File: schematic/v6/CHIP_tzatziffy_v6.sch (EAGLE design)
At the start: 51 parts, among them J1 2X20-CHIP0.8_DRILL, J3 S2B-PH-SM4-TB, Q1 NPN-DTC114YUA, Q2 PNP-DTA114YUA, U1 LMR62421, U3 DS2431P, X1 FH12-40S-0.5SH

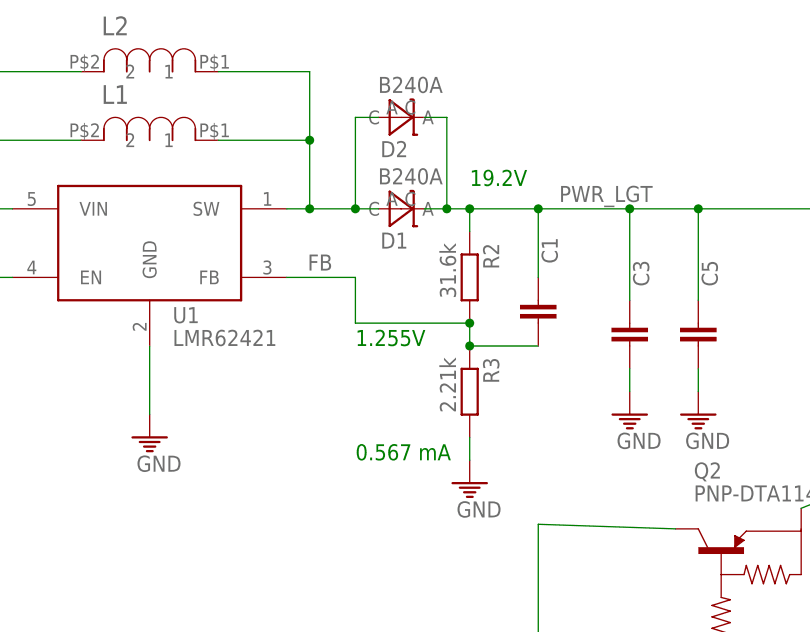
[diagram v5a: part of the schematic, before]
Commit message: added note for correct voltage divider
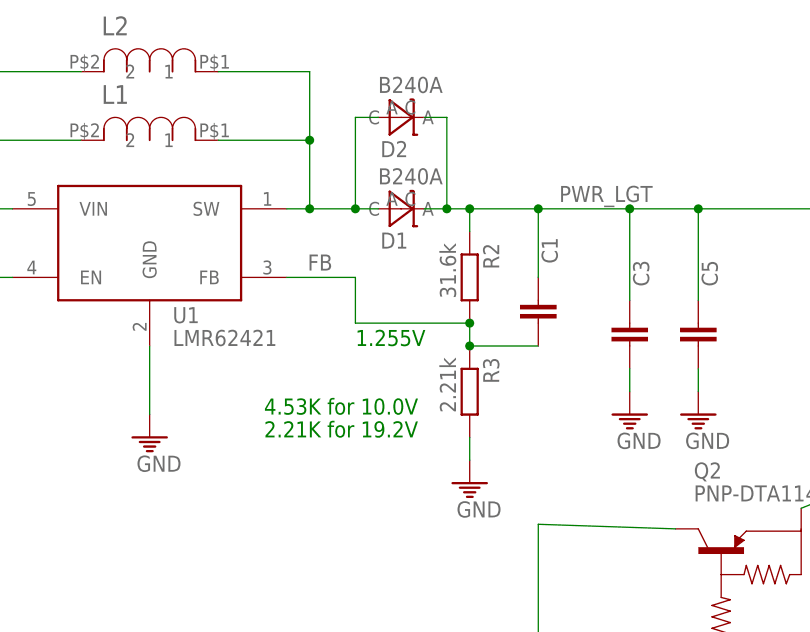
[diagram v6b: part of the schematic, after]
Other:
- note added: "2.21K for 19.2V"
- note added: "4.53K for 10.0V"
- note removed: "0.567 mA"
- note removed: "19.2V"
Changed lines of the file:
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@@
 <text x="236.22" y="81.28" size="1.778" layer="94" font="vector" ratio="12">1W EEPROM</text>
 <text x="530.86" y="246.38" size="1.778" layer="91">1.255V</text>
-<text x="543.56" y="264.16" size="1.778" layer="91">19.2V</text>
-<text x="530.86" y="233.68" size="1.778" layer="91">0.567 mA</text>
 <text x="363.22" y="246.38" size="1.778" layer="99">cut here</text>
 <text x="363.22" y="236.22" size="1.778" layer="99">cut here</text>
 <text x="449.58" y="243.84" size="1.778" layer="99" rot="R90">&lt;- cut here</text>
+<text x="520.7" y="238.76" size="1.778" layer="91">4.53K for 10.0V</text>
+<text x="520.7" y="236.22" size="1.778" layer="91">2.21K for 19.2V</text>
 </plain>
 <instances>

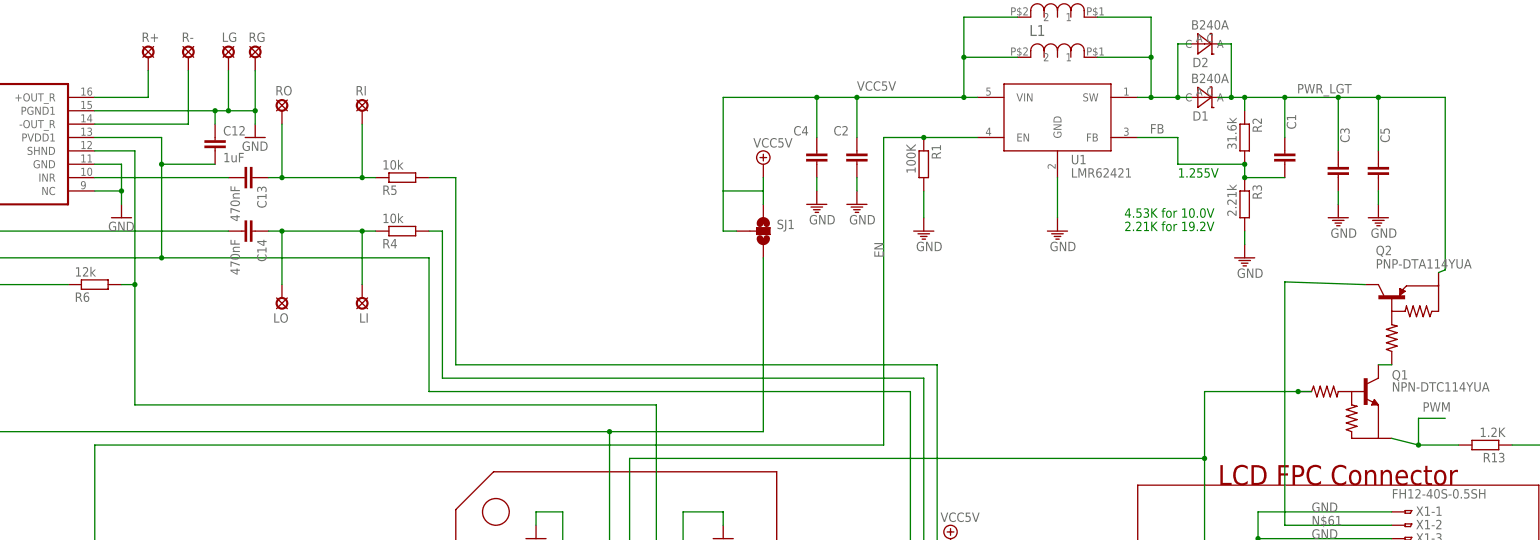
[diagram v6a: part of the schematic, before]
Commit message: changed 22uF Footprint to 1206
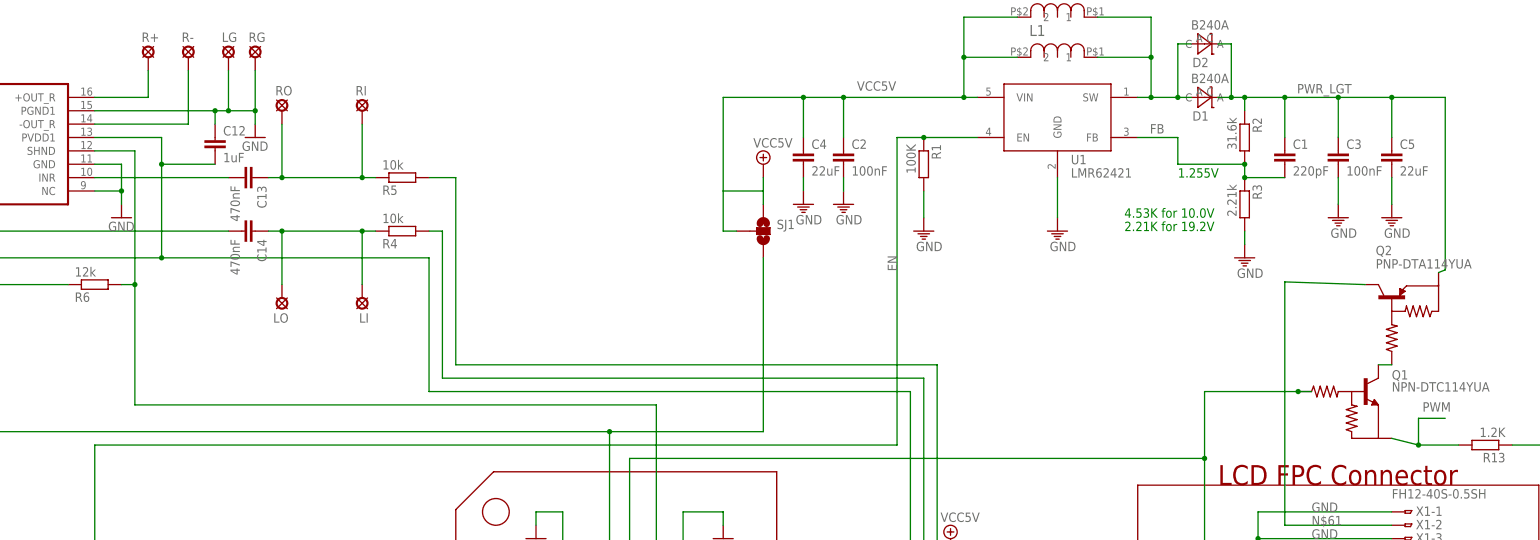
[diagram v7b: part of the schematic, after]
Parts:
- C4, C5: device rcl:C-EUC0805 -> rcl:C-EUC1206
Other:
- moved on the sheet: C2, C3, C4, C5
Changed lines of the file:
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@@
 <part name="U$13" library="Keyboard v0.2" deviceset="GND" device=""/>
 <part name="U$14" library="Keyboard v0.2" deviceset="GND" device=""/>
-<part name="C4" library="rcl" deviceset="C-EU" device="C0805" value="22uF"/>
-<part name="C5" library="rcl" deviceset="C-EU" device="C0805" value="22uF"/>
+<part name="C4" library="rcl" deviceset="C-EU" device="C1206" value="22uF"/>
+<part name="C5" library="rcl" deviceset="C-EU" device="C1206" value="22uF"/>
 <part name="U$15" library="Keyboard v0.2" deviceset="GND" device=""/>
 <part name="U$16" library="Keyboard v0.2" deviceset="GND" device=""/>
@@
 <instance part="U$8" gate="M" x="508" y="236.22"/>
 <instance part="U$12" gate="M" x="543.56" y="231.14"/>
-<instance part="C1" gate="G$1" x="551.18" y="251.46" smashed="yes">
-<attribute name="NAME" x="553.339" y="255.524" size="1.778" layer="95" rot="R90"/>
-</instance>
-<instance part="C2" gate="G$1" x="469.9" y="251.46" smashed="yes">
-<attribute name="NAME" x="468.376" y="256.159" size="1.778" layer="95" rot="R180"/>
-</instance>
-<instance part="C3" gate="G$1" x="561.34" y="248.92" smashed="yes">
-<attribute name="NAME" x="563.499" y="252.984" size="1.778" layer="95" rot="R90"/>
-</instance>
+<instance part="C1" gate="G$1" x="551.18" y="251.46"/>
+<instance part="C2" gate="G$1" x="467.36" y="251.46"/>
+<instance part="C3" gate="G$1" x="561.34" y="251.46"/>
 <instance part="U$13" gate="M" x="561.34" y="238.76"/>
-<instance part="U$14" gate="M" x="469.9" y="241.3"/>
-<instance part="C4" gate="G$1" x="462.28" y="251.46" smashed="yes">
-<attribute name="NAME" x="460.756" y="256.159" size="1.778" layer="95" rot="R180"/>
-</instance>
-<instance part="C5" gate="G$1" x="568.96" y="248.92" smashed="yes">
-<attribute name="NAME" x="571.119" y="252.984" size="1.778" layer="95" rot="R90"/>
-</instance>
-<instance part="U$15" gate="M" x="462.28" y="241.3"/>
-<instance part="U$16" gate="M" x="568.96" y="238.76"/>
+<instance part="U$14" gate="M" x="467.36" y="241.3"/>
+<instance part="C4" gate="G$1" x="459.74" y="251.46"/>
+<instance part="C5" gate="G$1" x="571.5" y="251.46"/>
+<instance part="U$15" gate="M" x="459.74" y="241.3"/>
+<instance part="U$16" gate="M" x="571.5" y="238.76"/>
 <instance part="L1" gate="G$1" x="500.38" y="269.24"/>
 <instance part="SUPPLY1" gate="+5V" x="487.68" y="177.8"/>
@@
 <segment>
 <pinref part="C3" gate="G$1" pin="2"/>
-<wire x1="561.34" y1="243.84" x2="561.34" y2="241.3" width="0.1524" layer="91"/>
+<wire x1="561.34" y1="246.38" x2="561.34" y2="241.3" width="0.1524" layer="91"/>
 <pinref part="U$13" gate="M" pin="GND"/>
 </segment>
@@
 <pinref part="C2" gate="G$1" pin="2"/>
 <pinref part="U$14" gate="M" pin="GND"/>
-<wire x1="469.9" y1="243.84" x2="469.9" y2="246.38" width="0.1524" layer="91"/>
+<wire x1="467.36" y1="243.84" x2="467.36" y2="246.38" width="0.1524" layer="91"/>
 </segment>
 <segment>
 <pinref part="C4" gate="G$1" pin="2"/>
 <pinref part="U$15" gate="M" pin="GND"/>
-<wire x1="462.28" y1="246.38" x2="462.28" y2="243.84" width="0.1524" layer="91"/>
+<wire x1="459.74" y1="246.38" x2="459.74" y2="243.84" width="0.1524" layer="91"/>
 </segment>
 <segment>
 <pinref part="U$16" gate="M" pin="GND"/>
 <pinref part="C5" gate="G$1" pin="2"/>
-<wire x1="568.96" y1="241.3" x2="568.96" y2="243.84" width="0.1524" layer="91"/>
+<wire x1="571.5" y1="241.3" x2="571.5" y2="246.38" width="0.1524" layer="91"/>
 </segment>
 <segment>
@@
 <pinref part="C3" gate="G$1" pin="1"/>
 <wire x1="551.18" y1="261.62" x2="561.34" y2="261.62" width="0.1524" layer="91"/>
-<wire x1="561.34" y1="261.62" x2="561.34" y2="251.46" width="0.1524" layer="91"/>
+<wire x1="561.34" y1="261.62" x2="561.34" y2="254" width="0.1524" layer="91"/>
 <junction x="551.18" y="261.62"/>
 <pinref part="C5" gate="G$1" pin="1"/>
-<wire x1="568.96" y1="251.46" x2="568.96" y2="261.62" width="0.1524" layer="91"/>
-<wire x1="568.96" y1="261.62" x2="561.34" y2="261.62" width="0.1524" layer="91"/>
+<wire x1="571.5" y1="254" x2="571.5" y2="261.62" width="0.1524" layer="91"/>
+<wire x1="571.5" y1="261.62" x2="561.34" y2="261.62" width="0.1524" layer="91"/>
 <junction x="561.34" y="261.62"/>
 <label x="563.88" y="264.16" size="1.778" layer="95" rot="R180"/>
-<wire x1="568.96" y1="261.62" x2="581.66" y2="261.62" width="0.1524" layer="91"/>
+<wire x1="571.5" y1="261.62" x2="581.66" y2="261.62" width="0.1524" layer="91"/>
 <wire x1="581.66" y1="261.62" x2="581.66" y2="228.854" width="0.1524" layer="91"/>
-<junction x="568.96" y="261.62"/>
+<junction x="571.5" y="261.62"/>
 <pinref part="D1" gate="G$1" pin="C"/>
 <wire x1="538.48" y1="261.62" x2="541.02" y2="261.62" width="0.1524" layer="91"/>
@@
 <wire x1="492.76" y1="261.62" x2="490.22" y2="261.62" width="0.1524" layer="91"/>
 <pinref part="C2" gate="G$1" pin="1"/>
-<wire x1="462.28" y1="261.62" x2="444.5" y2="261.62" width="0.1524" layer="91"/>
+<wire x1="459.74" y1="261.62" x2="444.5" y2="261.62" width="0.1524" layer="91"/>
 <pinref part="C4" gate="G$1" pin="1"/>
-<wire x1="462.28" y1="254" x2="462.28" y2="261.62" width="0.1524" layer="91"/>
-<junction x="462.28" y="261.62"/>
-<wire x1="462.28" y1="261.62" x2="469.9" y2="261.62" width="0.1524" layer="91"/>
-<wire x1="469.9" y1="261.62" x2="469.9" y2="254" width="0.1524" layer="91"/>
-<junction x="469.9" y="261.62"/>
-<wire x1="469.9" y1="261.62" x2="490.22" y2="261.62" width="0.1524" layer="91"/>
+<wire x1="459.74" y1="254" x2="459.74" y2="261.62" width="0.1524" layer="91"/>
+<junction x="459.74" y="261.62"/>
+<wire x1="459.74" y1="261.62" x2="467.36" y2="261.62" width="0.1524" layer="91"/>
+<wire x1="467.36" y1="261.62" x2="467.36" y2="254" width="0.1524" layer="91"/>
+<junction x="467.36" y="261.62"/>
+<wire x1="467.36" y1="261.62" x2="490.22" y2="261.62" width="0.1524" layer="91"/>
 <junction x="490.22" y="261.62"/>
 <wire x1="490.22" y1="269.24" x2="490.22" y2="261.62" width="0.1524" layer="91"/>
@@
 <pinref part="U1" gate="G$1" pin="EN"/>
 <wire x1="482.6" y1="254" x2="492.76" y2="254" width="0.1524" layer="91"/>
-<wire x1="482.6" y1="254" x2="474.98" y2="254" width="0.1524" layer="91"/>
+<wire x1="482.6" y1="254" x2="477.52" y2="254" width="0.1524" layer="91"/>
 <junction x="482.6" y="254"/>
-<label x="474.98" y="231.14" size="1.778" layer="95" rot="R90"/>
-<wire x1="325.12" y1="195.58" x2="474.98" y2="195.58" width="0.1524" layer="91"/>
-<wire x1="474.98" y1="195.58" x2="474.98" y2="254" width="0.1524" layer="91"/>
-</segment>
-<segment>
+<label x="477.52" y="228.6" size="1.778" layer="95" rot="R90"/>
+<wire x1="325.12" y1="195.58" x2="477.52" y2="195.58" width="0.1524" layer="91"/>
+<wire x1="477.52" y1="195.58" x2="477.52" y2="254" width="0.1524" layer="91"/>
+</segment>
+<segment>

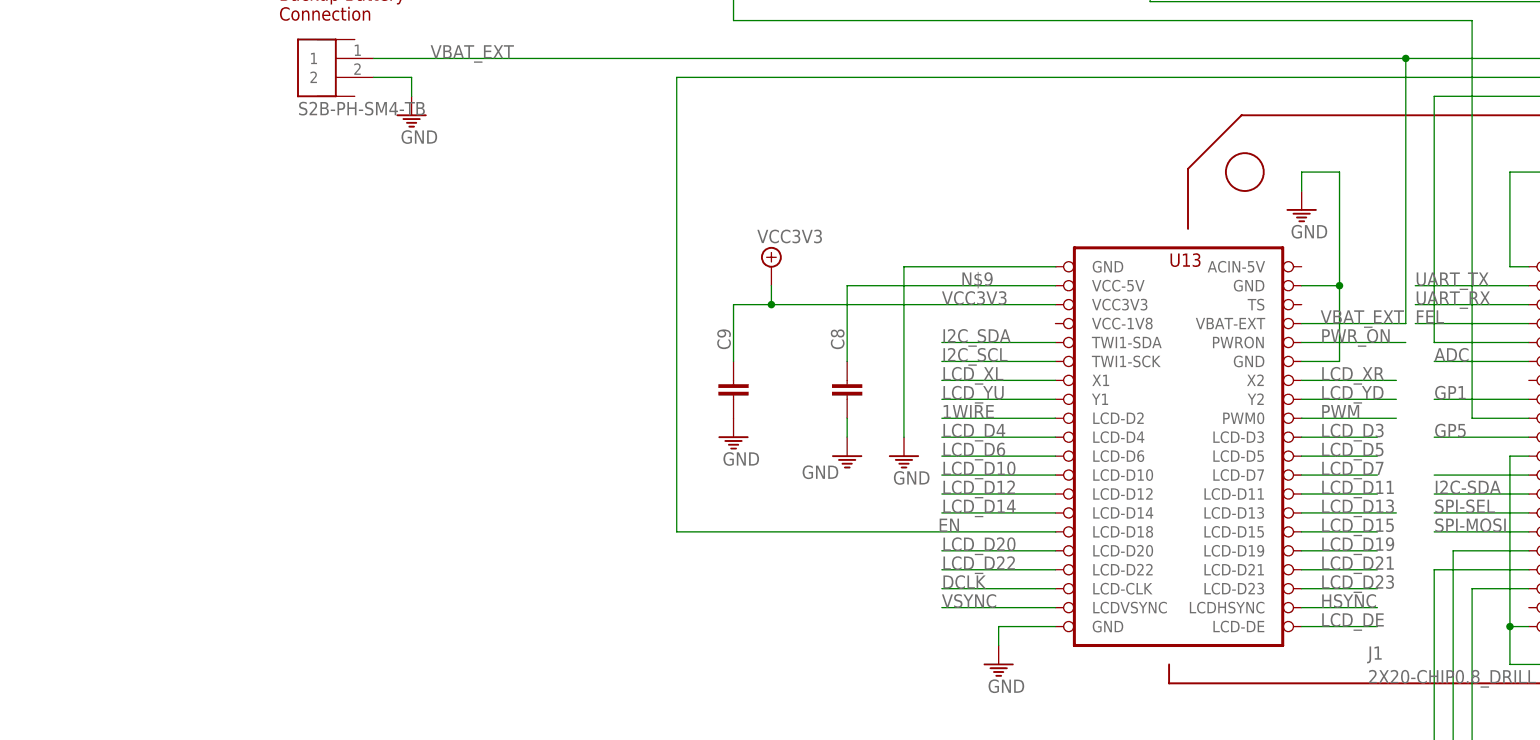
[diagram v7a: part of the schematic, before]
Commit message: Added pads for power button and vias for the uart header
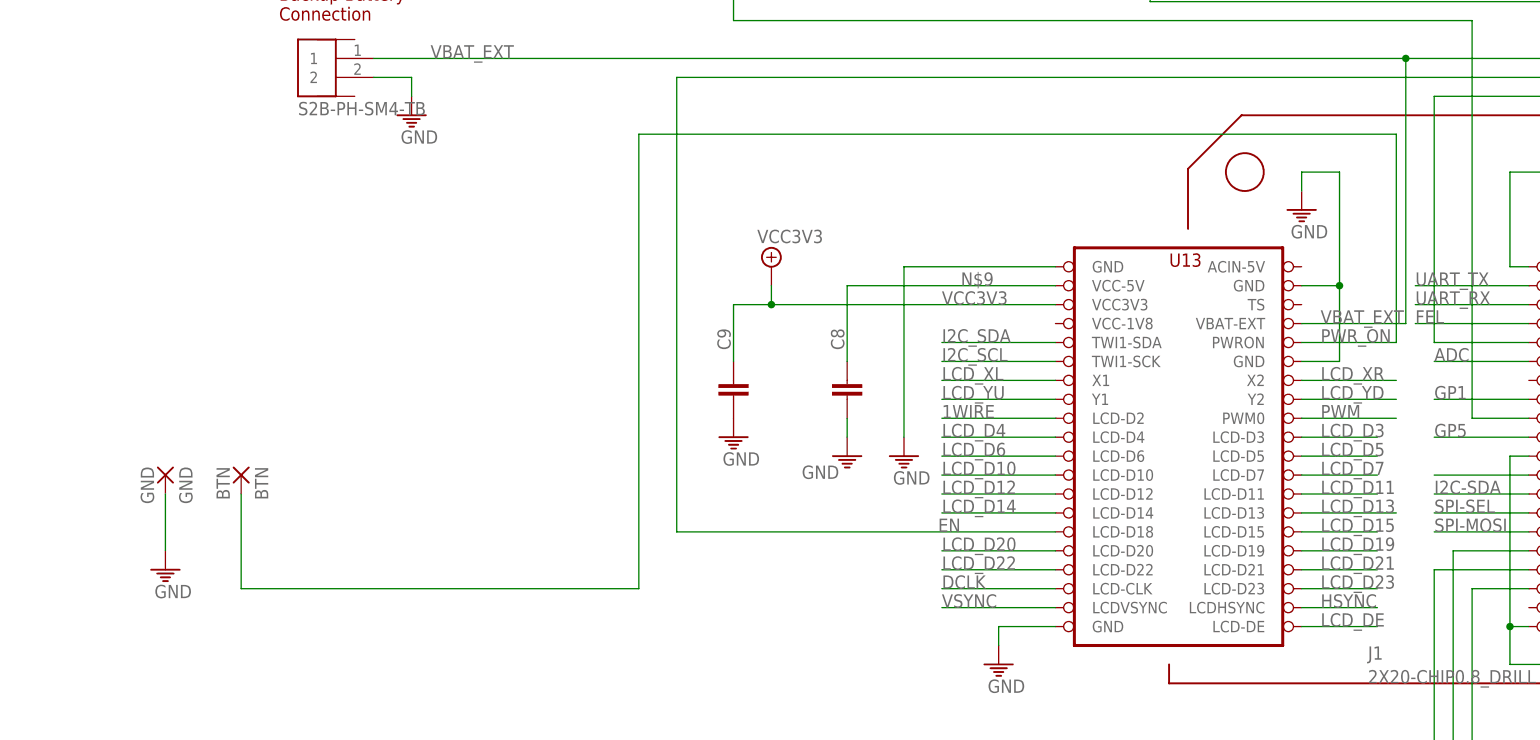
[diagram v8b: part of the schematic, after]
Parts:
- added BTN: BTN, wirepad:SMD5
- added GND: GND, wirepad:SMD5
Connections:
- net GND: now also GND.P
- net PWR_ON: now also BTN.P
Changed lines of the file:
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@@
 <part name="D2" library="Keyboard v0_5" deviceset="DIODE_SCHTKY_B240" device="" value="B240A"/>
 <part name="R6" library="rcl" deviceset="R-EU_" device="R0805" value="12k"/>
+<part name="GND" library="wirepad" deviceset="SMD5" device="" value="GND"/>
+<part name="BTN" library="wirepad" deviceset="SMD5" device="" value="BTN"/>
+<part name="U$6" library="Keyboard v0.2" deviceset="GND" device=""/>
 </parts>
 <sheets>
@@
 <instance part="D2" gate="G$1" x="535.94" y="271.78"/>
 <instance part="R6" gate="G$1" x="325.12" y="226.06" rot="MR180"/>
+<instance part="GND" gate="1" x="256.54" y="142.24" rot="R270"/>
+<instance part="BTN" gate="1" x="266.7" y="142.24" rot="R270"/>
+<instance part="U$6" gate="M" x="256.54" y="129.54"/>
 </instances>
 <busses>
@@
 <wire x1="472.44" y1="165.1" x2="480.06" y2="165.1" width="0.1524" layer="91"/>
 <wire x1="480.06" y1="165.1" x2="480.06" y2="160.02" width="0.1524" layer="91"/>
+</segment>
+<segment>
+<pinref part="U$6" gate="M" pin="GND"/>
+<pinref part="GND" gate="1" pin="P"/>
+<wire x1="256.54" y1="132.08" x2="256.54" y2="139.7" width="0.1524" layer="91"/>
 </segment>
 </net>
@@
 <net name="PWR_ON" class="0">
 <segment>
-<wire x1="408.94" y1="160.02" x2="422.91" y2="160.02" width="0.1524" layer="91"/>
+<wire x1="408.94" y1="160.02" x2="421.64" y2="160.02" width="0.1524" layer="91"/>
 <label x="411.48" y="160.02" size="1.778" layer="95" font="vector" ratio="12"/>
 <pinref part="J1" gate="G$1" pin="PWRON"/>
-</segment>
-</net>
+<wire x1="421.64" y1="160.02" x2="421.64" y2="187.96" width="0.1524" layer="91"/>
+<wire x1="421.64" y1="187.96" x2="320.04" y2="187.96" width="0.1524" layer="91"/>
+<wire x1="320.04" y1="187.96" x2="320.04" y2="127" width="0.1524" layer="91"/>
+<pinref part="BTN" gate="1" pin="P"/>
+<wire x1="320.04" y1="127" x2="266.7" y2="127" width="0.1524" layer="91"/>
+<wire x1="266.7" y1="127" x2="266.7" y2="139.7" width="0.1524" layer="91"/>
+</segment>
+</net>
